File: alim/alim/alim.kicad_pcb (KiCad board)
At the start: 2 copper layers, 50 x 50 mm, 32 parts, among them P1 CONN_2_PWR, P2 CONN_2_PWR, P3 CONN_2_PWR, P4 CONN_2_PWR, P5 CONN_2_PWR, Q1 BSC046N10NS3, Q2 BSC046N10NS3, Q3 BSC046N10NS3, Q4 BSC046N10NS3, U1 TPS5430DDA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

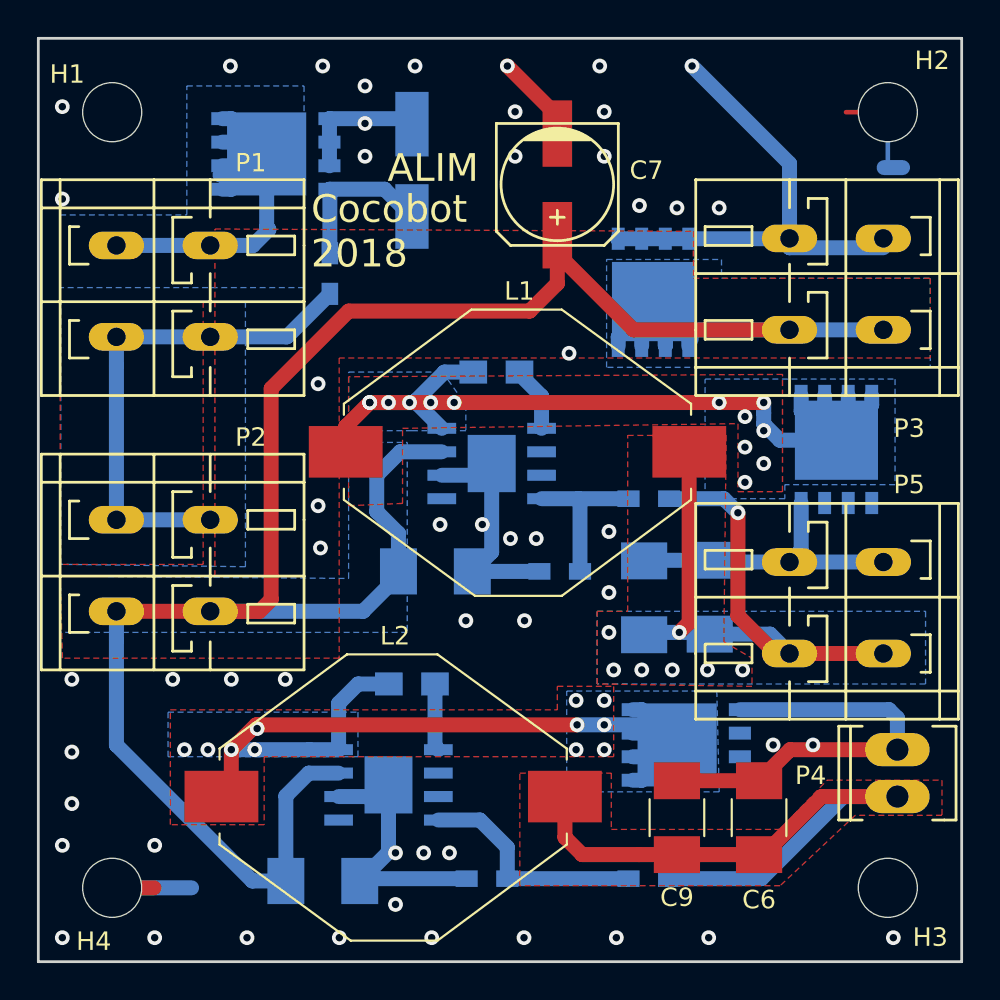
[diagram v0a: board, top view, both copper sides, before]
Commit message: add more infos on silk
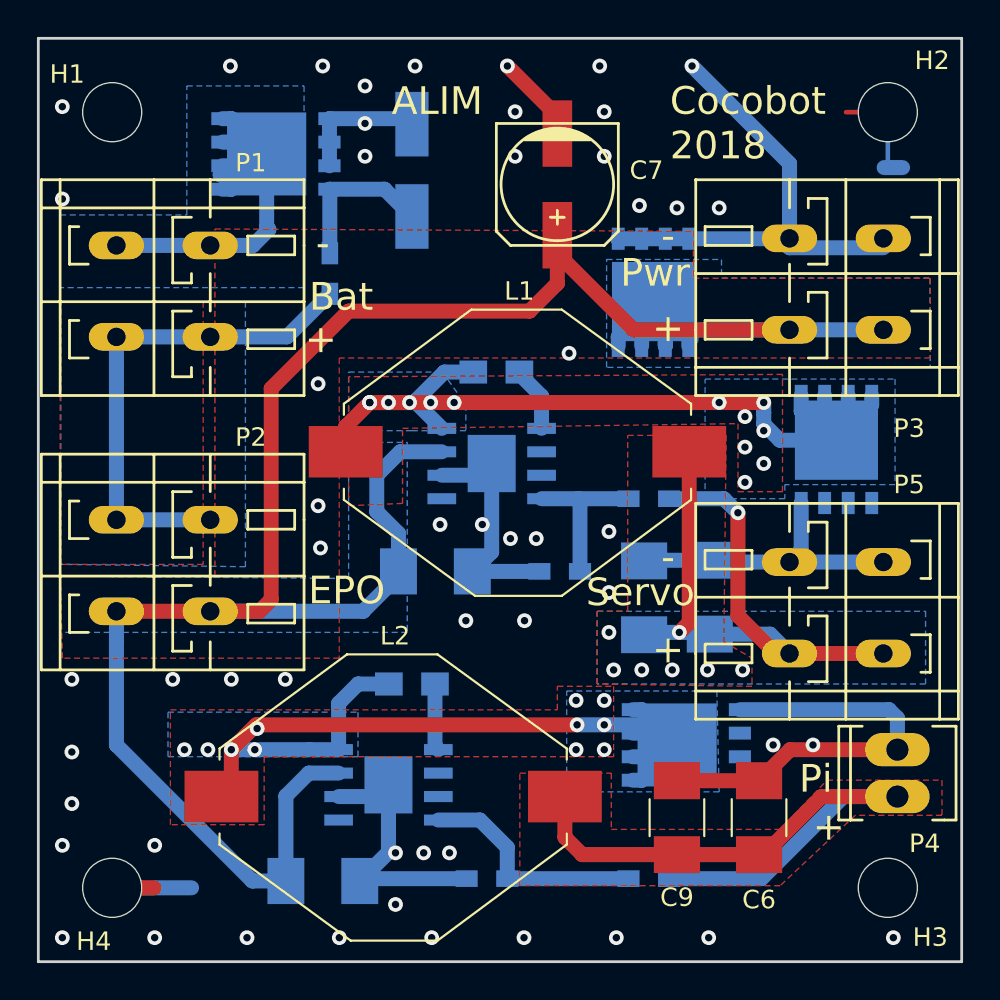
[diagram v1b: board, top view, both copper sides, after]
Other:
- board text added: "+"
- board text added: "-"
- board text added: "Bat"
- board text added: "EPO"
- board text added: "Pi"
- board text added: "Pwr"
- board text added: "Servo"
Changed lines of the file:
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@@
-(kicad_pcb (version 20171130) (host pcbnew "(2018-01-12 revision 650207a6e)-makepkg")
+(kicad_pcb (version 20171130) (host pcbnew "(2018-02-09 revision dba198e57)-master")
   (general
     (thickness 1.6)
-    (drawings 6)
+    (drawings 18)
     (tracks 271)
     (zones 0)
@@
     (visible_elements 7FFFFFFF)
     (pcbplotparams
-      (layerselection 0x010fc_ffffffff)
+      (layerselection 0x01020_7ffffffe)
       (usegerberextensions false)
       (usegerberattributes false)
@@
       (padsonsilk false)
       (subtractmaskfromsilk false)
-      (outputformat 1)
+      (outputformat 4)
       (mirror false)
-      (drillshape 1)
+      (drillshape 0)
       (scaleselection 1)
-      (outputdirectory ""))
+      (outputdirectory cmp/))
   )
   (net 0 "")
@@
     (descr "WAGO-Series 236, 2Stift, 2pol, RM 5mm,")
     (tags "WAGO-Series 236, 2Stift, 2pol, RM 5mm, Anreibare Leiterplattenklemme")
-    (fp_text reference P4 (at -9.144 -1.397) (layer F.SilkS)
+    (fp_text reference P4 (at -12.828 4.782) (layer F.SilkS)
       (effects (font (size 1 1) (thickness 0.15)))
     )
@@
       (net 1 GND))
   )
-  (gr_text "Cocobot\n2018" (at 64.77 60.452) (layer F.SilkS)
+  (gr_text + (at 92.8 92.7) (layer F.SilkS)
+    (effects (font (size 1.5 1.5) (thickness 0.3)))
+  )
+  (gr_text Pi (at 92.1 90.1) (layer F.SilkS)
+    (effects (font (size 1.5 1.5) (thickness 0.3)))
+  )
+  (gr_text - (at 84.1 78.1) (layer F.SilkS)
+    (effects (font (size 1.5 1.5) (thickness 0.3)))
+  )
+  (gr_text Servo (at 82.6 80) (layer F.SilkS)
+    (effects (font (size 1.5 1.5) (thickness 0.3)))
+  )
+  (gr_text + (at 84.1 83.1) (layer F.SilkS)
+    (effects (font (size 1.5 1.5) (thickness 0.3)))
+  )
+  (gr_text - (at 84.1 60.7) (layer F.SilkS)
+    (effects (font (size 1.5 1.5) (thickness 0.3)))
+  )
+  (gr_text + (at 84.1 65.7) (layer F.SilkS)
+    (effects (font (size 1.5 1.5) (thickness 0.3)))
+  )
+  (gr_text Pwr (at 83.4 62.7) (layer F.SilkS)
+    (effects (font (size 1.5 1.5) (thickness 0.3)))
+  )
+  (gr_text EPO (at 66.7 79.9) (layer F.SilkS)
+    (effects (font (size 1.5 1.5) (thickness 0.3)))
+  )
+  (gr_text Bat (at 66.4 64) (layer F.SilkS)
+    (effects (font (size 1.5 1.5) (thickness 0.3)))
+  )
+  (gr_text - (at 65.4 61.1) (layer F.SilkS)
+    (effects (font (size 1.5 1.5) (thickness 0.3)))
+  )
+  (gr_text + (at 65.3 66.3) (layer F.SilkS)
+    (effects (font (size 1.5 1.5) (thickness 0.3)))
+  )
+  (gr_text "Cocobot\n2018" (at 84.2 54.6) (layer F.SilkS)
     (effects (font (size 1.5 1.5) (thickness 0.3)) (justify left))
   )
-  (gr_text ALIM (at 71.374 57.023) (layer F.SilkS)
+  (gr_text ALIM (at 71.6 53.4) (layer F.SilkS)
     (effects (font (size 1.5 1.5) (thickness 0.3)))
   )
